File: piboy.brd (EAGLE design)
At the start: 76.2 x 76.2 mm, 75 parts, among them CN4 MicroUSB, T1 MMUN2133LT1G, U1 TPS61090RSAR, U2 MCP73871

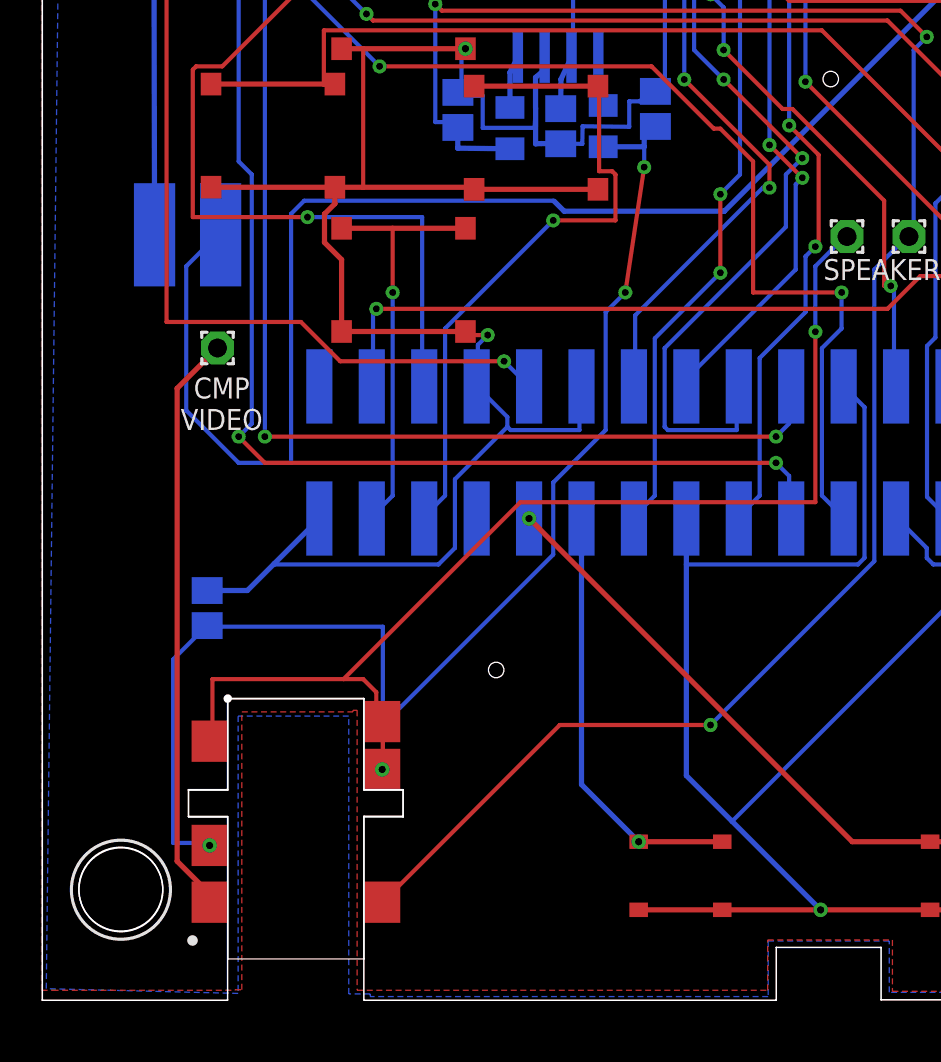
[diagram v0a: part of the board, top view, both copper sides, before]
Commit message: -moved headphone jack down by 5 mm to make it easier to plug in
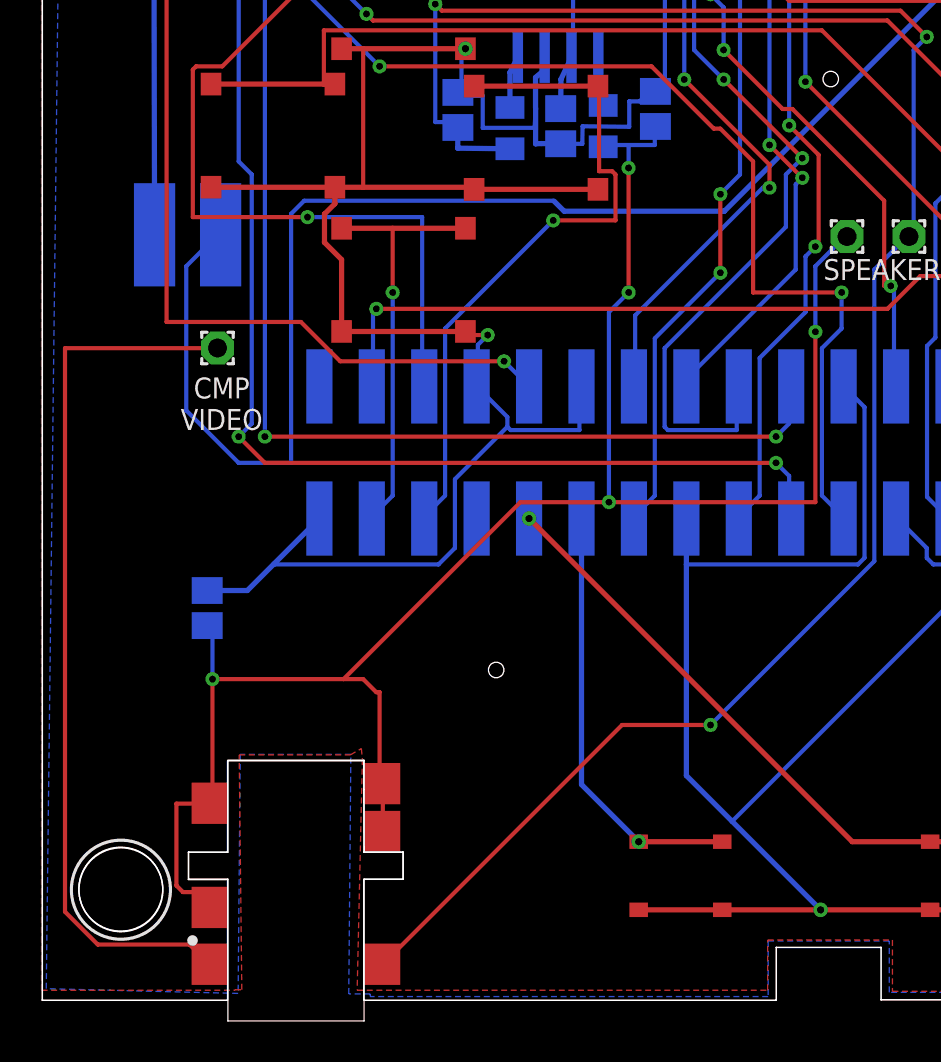
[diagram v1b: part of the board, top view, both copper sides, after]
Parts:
- moved U$40 3.01 mm to (15.6, -1.01)
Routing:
- net AUD+: track 120.0 -> 92.7 mm
- net CMP_VIDEO_OUT: track 28.3 -> 42.8 mm
- net AUD-: track 92.2 -> 93.4 mm
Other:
- outline, holes or cut-outs redrawn

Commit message: -connected IN- in amp input to ground
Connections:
- removed net N$26: C12.2, U$33.P$1
- net GND: now also C12.2, U$33.P$1
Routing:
- net GND: track 506.3 -> 521.4 mm
- net N$26: track 15.1 -> 0.00 mm
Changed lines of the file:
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@@
 <vertex x="-0.0254" y="72.39"/>
 </polygon>
+<contactref element="C12" pad="2"/>
+<contactref element="U$33" pad="P$1"/>
+<wire x1="25.8171" y1="58.6668" x2="25.842075" y2="58.8538" width="0.254" layer="16"/>
+<wire x1="25.842075" y1="58.8538" x2="25.956175" y2="59.743" width="0.254" layer="16"/>
+<wire x1="25.956175" y1="59.743" x2="12.703" y2="59.743" width="0.254" layer="16"/>
+<wire x1="12.703" y1="59.743" x2="12.26" y2="59.3" width="0.254" layer="16"/>
+<wire x1="12.26" y1="59.3" x2="12.1" y2="59.3" width="0.254" layer="16"/>
+<wire x1="65.2914" y1="55.5932" x2="73.4583" y2="51.2084" width="0" layer="19" extent="16-16"/>
+<wire x1="25.956175" y1="59.743" x2="26.51125" y2="61.75375" width="0" layer="19" extent="16-16"/>
+<wire x1="71.3894" y1="38.252" x2="67.617" y2="41.718" width="0" layer="19" extent="1-16"/>
+<wire x1="66.6693" y1="19.0663" x2="72.1684" y2="20.6284" width="0" layer="19" extent="1-1"/>
 </signal>
 <signal name="N$1">
@@
 <wire x1="13.7787" y1="58.5342" x2="12.1" y2="57.3" width="0.254" layer="16"/>
 </signal>
-<signal name="N$26">
-<contactref element="C12" pad="2"/>
-<contactref element="U$33" pad="P$1"/>
-<wire x1="25.8171" y1="58.6668" x2="25.842075" y2="58.8538" width="0.254" layer="16"/>
-<wire x1="25.842075" y1="58.8538" x2="25.956175" y2="59.743" width="0.254" layer="16"/>
-<wire x1="25.956175" y1="59.743" x2="12.703" y2="59.743" width="0.254" layer="16"/>
-<wire x1="12.703" y1="59.743" x2="12.26" y2="59.3" width="0.254" layer="16"/>
-<wire x1="12.26" y1="59.3" x2="12.1" y2="59.3" width="0.254" layer="16"/>
-</signal>
 <signal name="AO-">

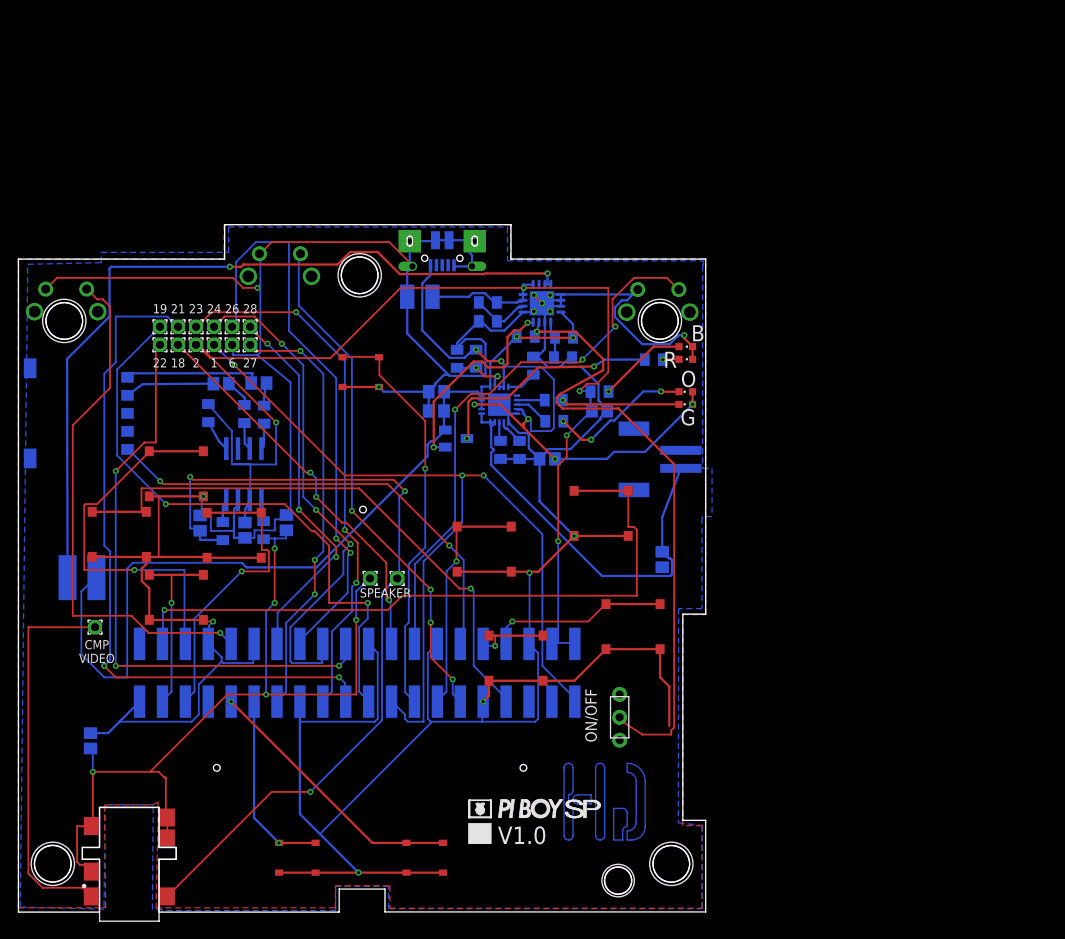
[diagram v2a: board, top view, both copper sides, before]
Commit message: -Created a new board revision 1.1 -moved layout of the screen pins -relocated the audio circuit
TODO
-Relocate the power circuit
-Fix the button smd pads
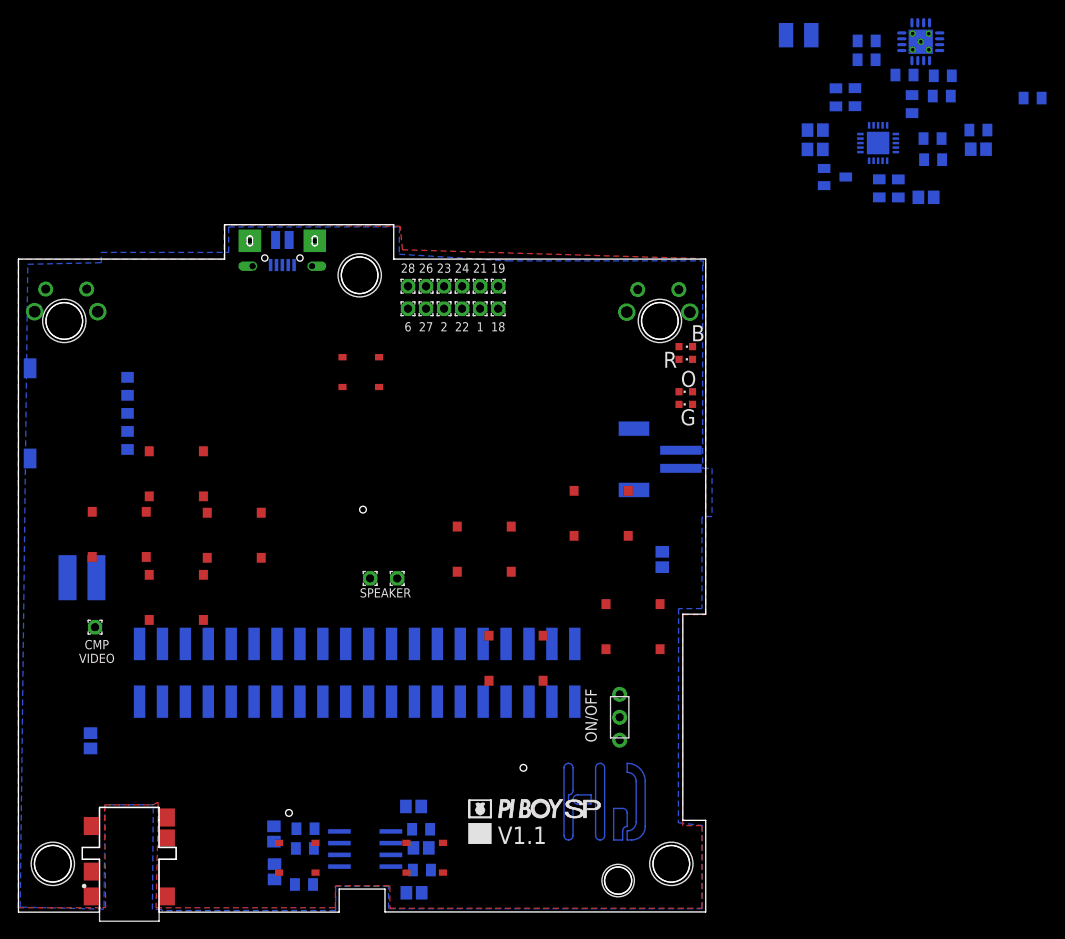
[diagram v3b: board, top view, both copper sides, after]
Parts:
- removed U$30: SWITCH_TL1105L-4,3, piboy_new:SWITCH_TL1105L-4,3
- moved C11 54.4 mm to (28.4, 4.48), turned to 270 degrees
- moved R22 53.3 mm to (31.7, 3.06), turned to 180 degrees
- moved R3 51.0 mm to (94.1, 96.6)
- moved R6 51.0 mm to (92.8, 90.4)
- moved R8 51.0 mm to (101.4, 83.4)
- moved C1 51.0 mm to (88.3, 84.6)
- moved C2 51.0 mm to (106.4, 84.6)
- moved C4 51.0 mm to (88.3, 86.7)
- moved C6 51.0 mm to (86.5, 97.2)
- moved C8 51.0 mm to (100.6, 79.3)
- moved R1 51.0 mm to (102.5, 92.7)
- moved R13 51.0 mm to (98.3, 92.8)
- moved R14 51.0 mm to (101.4, 85.8)
- moved R16 51.0 mm to (95.5, 80.3)
- moved R17 51.0 mm to (97.6, 80.2)
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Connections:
- net GND: no longer U$30.2
- net J_ESC: no longer U$30.1
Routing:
- net GND: track 521.4 -> 0.00 mm, vias 9 -> 0
- net 5.0V: track 148.5 -> 0.00 mm, vias 5 -> 0
- net 3.3V: track 99.0 -> 0.00 mm, vias 3 -> 0
- net VBAT: track 97.4 -> 0.00 mm, vias 2 -> 0
- net AUD-: track 93.4 -> 0.00 mm, vias 3 -> 0
- net AUD+: track 92.7 -> 0.00 mm, vias 5 -> 0
- net N$1: track 88.5 -> 0.00 mm, vias 2 -> 0
- net MISO: track 76.7 -> 0.00 mm, vias 2 -> 0
- net J_X: track 75.3 -> 0.00 mm, vias 1 -> 0
- net VBUS: track 73.1 -> 0.00 mm, vias 6 -> 0
- net ENABLE: track 70.9 -> 0.00 mm, vias 1 -> 0
- net MOSI: track 66.3 -> 0.00 mm, vias 2 -> 0
- net TFT_DC: track 66.1 -> 0.00 mm, vias 3 -> 0
- net RT_CS: track 63.9 -> 0.00 mm, vias 2 -> 0
- net J_LFT: track 63.9 -> 0.00 mm, vias 1 -> 0
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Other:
- outline, holes or cut-outs redrawn
- board text added: "V1.1"
- board text removed: "V1.0"

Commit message: -routed power circuit -routed SPI pinouts TODO -Clean up schematic: replace parts with parts that have labels, replace similar parts with all parts from the same library
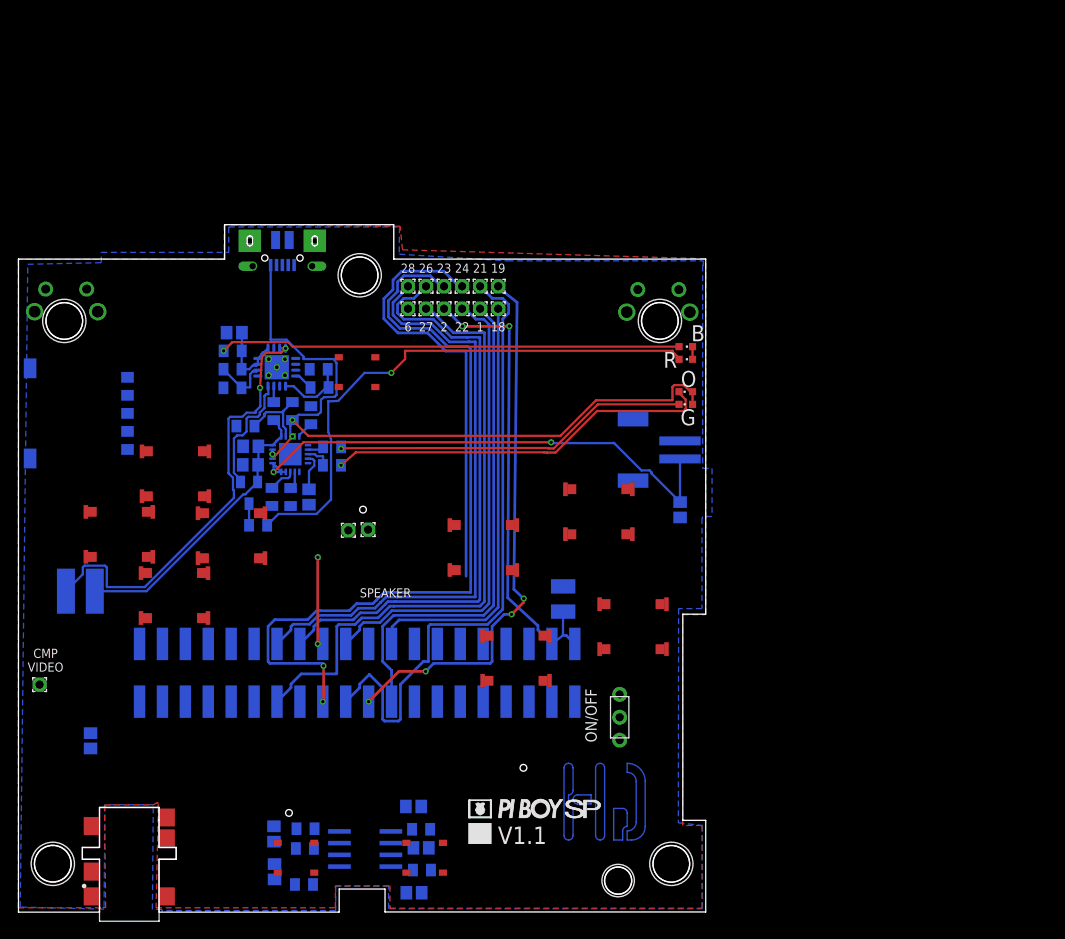
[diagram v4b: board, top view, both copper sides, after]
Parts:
- B1: device microbuilder:JSTPH2 -> piboy_new:MICROBUILDER_JSTPH2_NOTHERMALS
- U$10, U$11, U$12, U$13, U$15, U$16, U$17, U$18: value SKRRAAE010 -> PIBOY_SKRRAAE010; device piboy:SKRRAAE010 -> piboy_new:PIBOY_SKRRAAE010
- moved R20 98.1 mm to (26.6, 42.9)
- moved R5 86.2 mm to (23.8, 62.2), turned to 0 degrees
- moved C2 85.0 mm to (23.9, 64.3), turned to 0 degrees
- moved U1 80.0 mm to (28.7, 60.4)
- moved R13 79.2 mm to (28.3, 55.6), turned to 90 degrees
- moved R3 79.2 mm to (23.7, 60.2)
- moved R4 79.2 mm to (23.7, 58.1)
- moved R1 77.3 mm to (33.4, 58.2), turned to 0 degrees
- moved C8 76.1 mm to (32.2, 46.0), turned to 270 degrees
- moved R17 75.6 mm to (30.2, 46.0)
- moved R16 75.5 mm to (28.1, 46.0)
- moved R2 75.4 mm to (33.3, 60.2), turned to 180 degrees
- moved THERM 75.0 mm to (32.4, 55.1)
- moved R7 74.9 mm to (25.2, 53.9), turned to 0 degrees
- moved R14 74.8 mm to (34.8, 51.6)
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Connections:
- net GND: now also B1.NC1, B1.NC2, U$33.GND1, U$33.GND2
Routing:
- net VBUS: track 0.00 -> 88.2 mm, vias 0 -> 3
- net SCLK: track 0.00 -> 86.2 mm, vias 0 -> 2
- net MISO: track 0.00 -> 70.8 mm
- net EEDATA: track 0.00 -> 68.3 mm
- net EECLK: track 0.00 -> 66.9 mm
- net RT_CS: track 0.00 -> 66.5 mm
- net N$2: track 0.00 -> 61.5 mm, vias 0 -> 1
- net MOSI: track 0.00 -> 60.6 mm, vias 0 -> 4
- net TFT_CS: track 0.00 -> 59.8 mm, vias 0 -> 2
- net 5.0V: track 0.00 -> 59.7 mm, vias 0 -> 2
- net VLIPO: track 0.00 -> 57.9 mm, vias 0 -> 2
- net 3.3V: track 0.00 -> 55.7 mm
- net TFT_DC: track 0.00 -> 52.6 mm
- net N$4: track 0.00 -> 51.1 mm, vias 0 -> 1
- net N$1: track 0.00 -> 49.0 mm, vias 0 -> 2
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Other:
- board text added: "+"
- board text removed: "C1"
- board text removed: "C4"
- board text removed: "C6"
- board text removed: "C8"
- board text removed: "R1"
- board text removed: "R13"
- board text removed: "R14"
- board text removed: "R16"
- board text removed: "R17"
- board text removed: "R2"
- board text removed: "R20"
- board text removed: "R3"
- board text removed: "R4"
- board text removed: "R5"
- board text removed: "R6"
- board text removed: "R7"
- board text removed: "R8"
- board text removed: "THM"

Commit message: -*finally* think I solved the audio issue, redid audio schematic with new parts -started layout
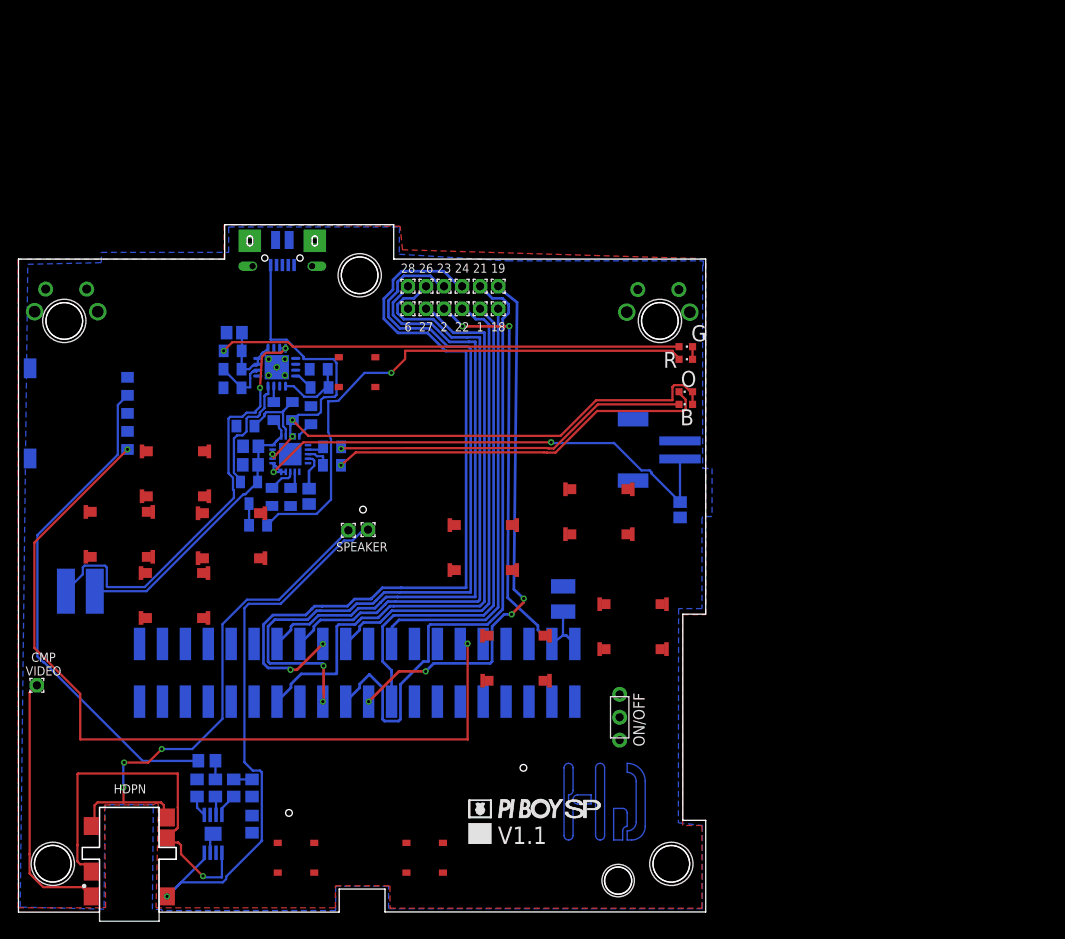
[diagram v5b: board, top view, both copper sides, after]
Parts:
- removed C11, C12: 1uf, piboy_new:ADAFRUIT_C0805
- removed C13: 10uf, piboy_new:ADAFRUIT_C0805
- removed C14, C15: 220pf, piboy_new:ADAFRUIT_C0805
- removed FB1, FB2: 100 Ohm @ 100 Mhz, piboy_new:ADAFRUIT_R0805
- removed R19, R21: 100, piboy_new:ADAFRUIT_R0805
- removed R22: 10k, piboy_new:ADAFRUIT_R0805
- removed U$31: PAM8302A, piboy_new:PAM8302A
- added C5: 1uF, resistor:C0805
- added C9: 10uF, resistor:C0805
- added R10, R11: 150K, resistor:R0805
- added R9: 10K, resistor:R0805
- added U3: TPA2005D1, SparkFun-IC-Amplifiers:POWER-SOP8
- C3: value 100nf -> 1uF; device piboy_new:ADAFRUIT_C0805 -> resistor:C0805
- C8: value 10uF -> 10uf; device piboy_new:ADAFRUIT_C0805 -> adafruit:C0805
- moved C3 16.7 mm to (23.9, 13.8), turned to 270 degrees
- moved CMP_VIDEO_OUT 0.31 mm to (2.05, 25.1)
- moved C8 0.07 mm to (32.2, 46.1)
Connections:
- removed net AIN+: R19.2, U$31.P$3
- removed net AIN-: R21.2, U$31.P$4
- removed net AO+: FB2.1, U$31.P$5
- removed net AO-: FB1.1, U$31.P$8
- removed net J_ESC: U$9.P11
- removed net J_VUP: U$9.P40
- removed net N$25: C11.2, U$33.P$2
- removed net SD: R22.2, U$31.P$1
- new net AUD+_HDPN_OUT: SPK2.1, U$40.P$5, U$40.P$6
- new net N$21: C3.1, R11.2
- new net N$22: R10.1, U$33.P$2
- new net N$23: C5.2, U3.3
- new net N$26: C3.2, U3.4
- net 5.0V: now also C9.2, R9.1, U3.6; no longer C13.1, R22.1, U$31.P$6
- net AUD+: now also U3.5; no longer C14.1, C3.1, FB2.2, SPK2.1, U$40.P$5, U$40.P$6
- net AUD-: now also U3.8; no longer C15.1, FB1.2
- net GND: now also C9.1, R11.1, U3.7, U3.9; no longer C12.2, C13.2, C14.2, C15.2, C3.2, U$31.P$7
- net J_RGT: now also U$9.P11; no longer U$9.P35
- net N$17: now also R9.2, U3.1; no longer C12.1, R21.1
- net N$20: now also C5.1, R10.2; no longer C11.1, R19.1
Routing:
- net PWM0: track 0.00 -> 93.0 mm, vias 0 -> 2
- net AUD-: track 0.00 -> 64.2 mm, vias 0 -> 1
- net AUD+_HDPN_OUT: track 0.00 -> 58.7 mm, vias 0 -> 3
- net N$22: track 0.00 -> 55.7 mm
- net AUD+: track 0.00 -> 41.8 mm, vias 0 -> 1
- net CMP_VIDEO_OUT: track 0.00 -> 29.1 mm
- net TFT_CS: track 59.8 -> 86.9 mm
- net N$26: track 0.00 -> 2.57 mm
- net N$17: track 0.00 -> 2.36 mm
- net GND: track 1.40 -> 3.63 mm
- net N$20: track 0.00 -> 2.07 mm
- net N$23: track 0.00 -> 2.06 mm
- net N$21: track 0.00 -> 2.03 mm
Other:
- board text added: "HDPN"
- board text added: "USB CHRG"
- board text removed: "C11"
- board text removed: "C12"
- board text removed: "C13"
- board text removed: "C14"
- board text removed: "C15"
- board text removed: "C2"
- board text removed: "C3"
- board text removed: "C7"
- board text removed: "FB1"
- board text removed: "FB2"
- board text removed: "R19"
- board text removed: "R21"
- board text removed: "R22"
